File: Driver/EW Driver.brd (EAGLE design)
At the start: 114.3 x 81.3 mm, 42 parts, among them Q1 IRF840S, U1 MAX1771ESA, U2 ARDUINOMICRO, U5 HV507, U6 HV507, X1 BNCHOR

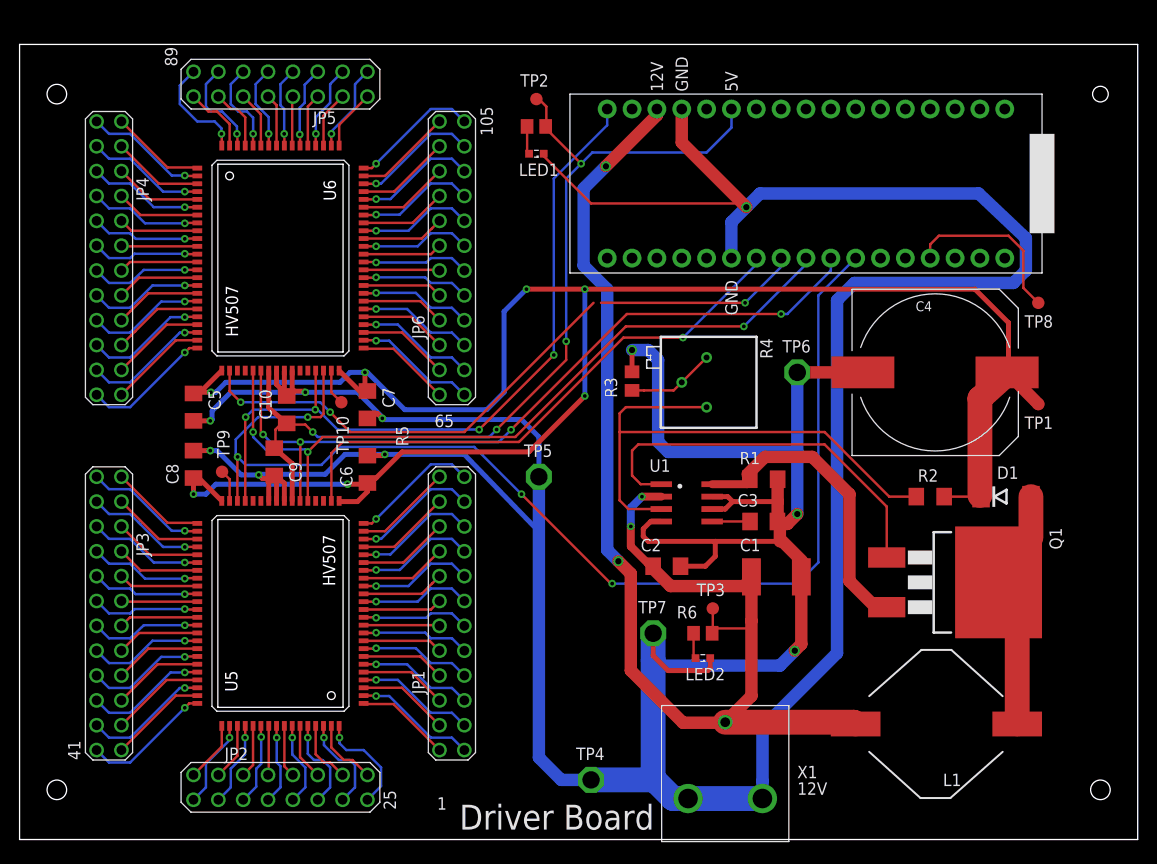
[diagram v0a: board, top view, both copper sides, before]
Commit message: HV traces reduced to 6 mils. Silkscreen added for both boards.
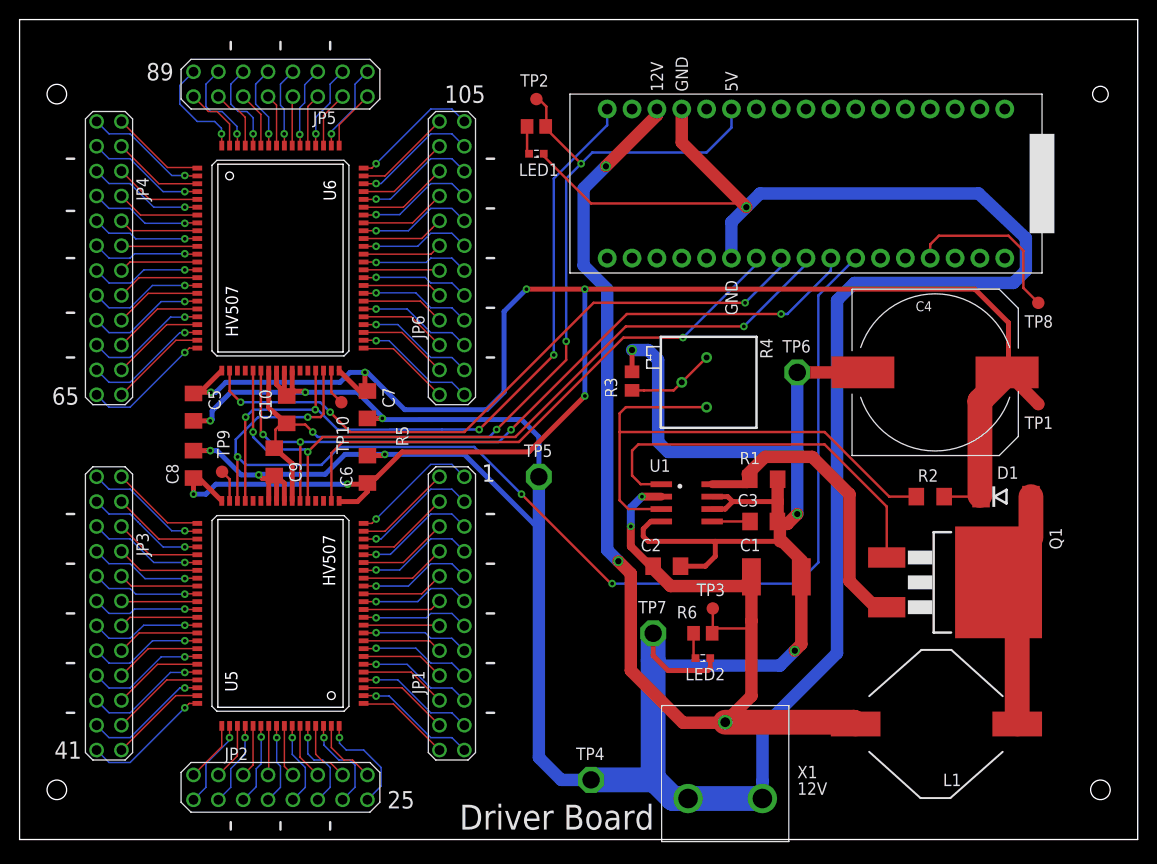
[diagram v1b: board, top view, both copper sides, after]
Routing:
- net DIA_2: track 67.3 -> 68.1 mm
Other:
- board size 114.3 x 81.3 mm -> 114.3 x 83.8 mm
